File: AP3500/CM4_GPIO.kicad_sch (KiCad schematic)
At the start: 12 parts, among them J9 0826-1X1T-GH-F, U1 TPD4EUSB30, U2 TPD4EUSB30, U5 74LVC1G07SE-7

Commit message: Finalize AP3500 board
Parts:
- added D19, D20, D21, D22, D23, D3: LED Green, LED_SMD:LED_0603_1608Metric, symbol Device:LED
- added J1: Console, Connector_PinHeader_2.54mm:PinHeader_1x04_P2.54mm_Vertical, symbol Connector_Generic:Conn_01x04
- added R19, R20, R36, R39, R6, R7: 1K 1%, Resistor_SMD:R_0603_1608Metric, symbol Device:R
- added U3: SN74LVC07AD, Package_SO:SOIC-14_3.9x8.7mm_P1.27mm, symbol 2021-01-22_15-06-37:SN74LVC07AD
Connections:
- net +3.3v: now also D19.2 (A), D20.2 (A), D21.2 (A), D22.2 (A), D23.2 (A), D3.2 (A), J1.1 (Pin_1), U3.14 (VCC)
- net GND: now also J1.4 (Pin_4), U3.7 (GND)
- net GPIO17: now also U3.9 (4A)
- net GPIO2: now also U3.1 (1A)
- net GPIO22: now also U3.13 (6A)
- net GPIO27: now also U3.11 (5A)
- net GPIO3: now also U3.3 (2A)
- net GPIO4: now also U3.5 (3A)
- net GPIO14 renamed UART_TX
- net UART_TX: now also J1.2 (Pin_2)
- net GPIO15 renamed UART_RX
- net UART_RX: now also J1.3 (Pin_3)
- new net: R36.1, U3.10 (5Y)
- new net: R39.1, U3.12 (6Y)
- new net: R6.1, U3.2 (1Y)
- new net: R7.1, U3.4 (2Y)
- new net: R19.1, U3.6 (3Y)
- new net: R20.1, U3.8 (4Y)
- new net: D22.1 (K), R36.2
- new net: D23.1 (K), R39.2
- new net: D3.1 (K), R6.2
- new net: D21.1 (K), R20.2
- new net: D19.1 (K), R7.2
- new net: D20.1 (K), R19.2
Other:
- note added: "RSSI1 LED"
- note added: "RSSI2 LED"
- note added: "RSSI3 LED"
- note added: "RSSI4 LED"
- note added: "RSSI5 LED"
- note added: "USR LED"

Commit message: More work on Antennas - laying out the new panel as a 2x2 aperture coupled patch
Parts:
- C1: value 100n 16v -> 100n 50v; LCSC (none) -> C14663; PartsBoxID 0603-100nF-X7R-16V -> 0603-100nF-X7R-50V
- D1: LCSC (none) -> C125094; PartsBoxID LTST-S270KRKT -> 0603-LED-RED
- D19, D2, D20, D21, D22, D23, D3: LCSC (none) -> C125094; PartsBoxID LTST-S270KGKT -> 0603-LED-GREEN
- R1, R10, R19, R20, R36, R39, R6, R7: LCSC (none) -> C21190
- R2, R3: LCSC (none) -> C23179
- U3: LCSC (none) -> C7659; PartsBoxID (none) -> SN74LVC07AD
- U5: LCSC (none) -> C7829

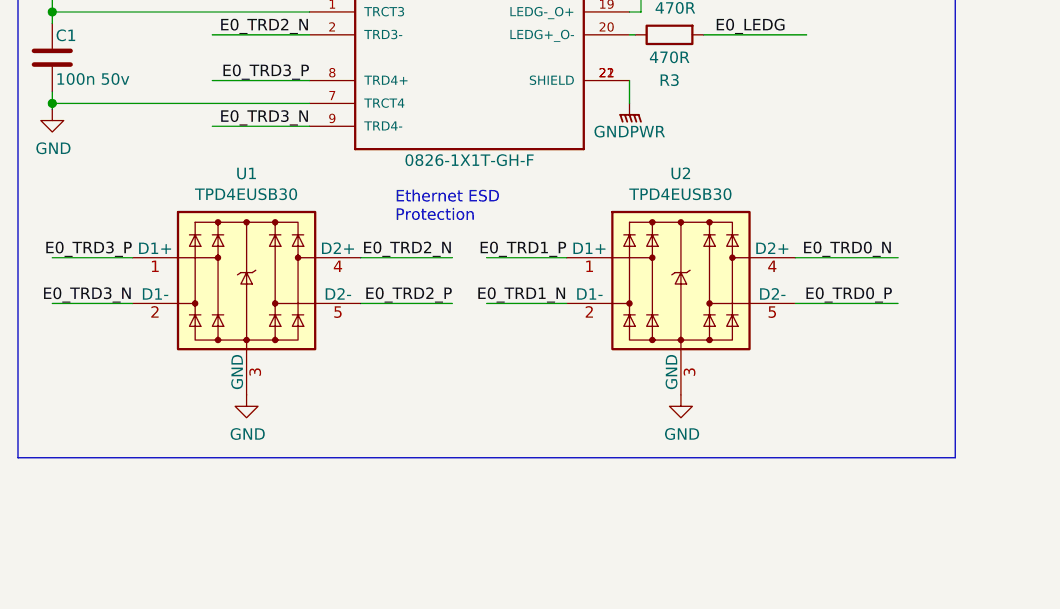
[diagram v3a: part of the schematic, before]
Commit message: Add new single polarity aperture coupled 4x4 antenna. RasPiCNM4Connector test Gerbers for PCBWay Cleanups and optimixations for AP3500
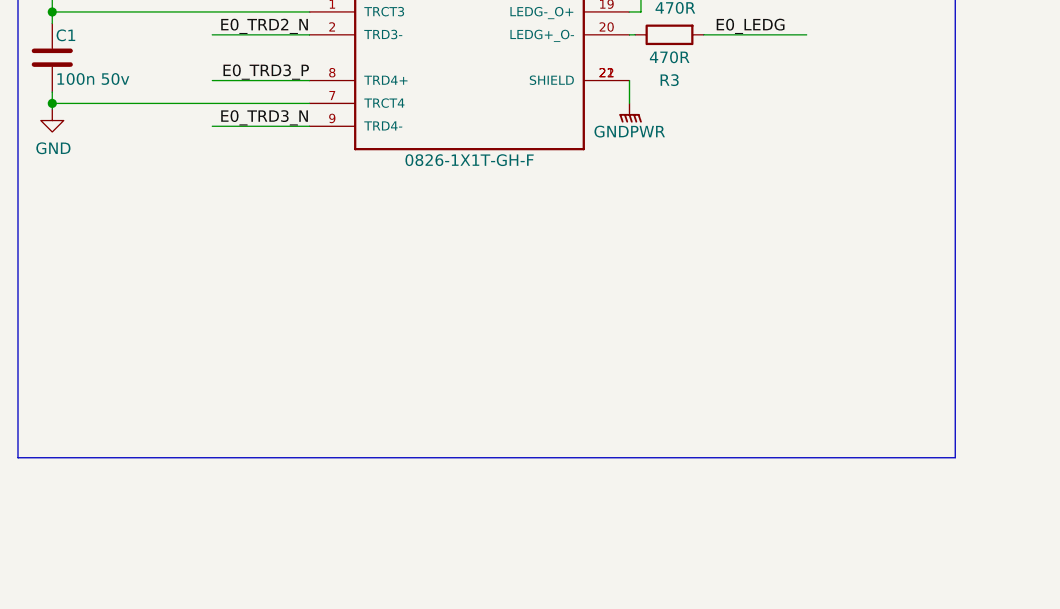
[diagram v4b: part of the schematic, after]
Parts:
- removed U1, U2: TPD4EUSB30, Scott:USON-10_2.51x1.0mm_P0.5mm, symbol AP3500:TPD4EUSB30
- C1: PartsBoxID 0603-100nF-X7R-50V -> (none)
- D1: PartsBoxID 0603-LED-RED -> (none)
- D19, D2, D20, D21, D22, D23, D3: PartsBoxID 0603-LED-GREEN -> (none)
- Module1: footprint AP3500:Raspberry-Pi-4-Compute-Module -> AP3000:Raspberry-Pi-4-Compute-Module; now left out of the parts list
- R1, R10, R19, R20, R36, R39, R6, R7: PartsBoxID 0603-1K-1% -> (none)
- R2, R3: PartsBoxID 0603-470R-1% -> (none)
- U5: PartsBoxID 74LVC1G07SE-7 -> (none)
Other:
- note removed: "Ethernet ESD Protection"

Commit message: Updates for JLCPCB components actually in stock at this time
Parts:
- D1: LCSC C125094 -> C2286
- D19, D2, D20, D21, D22, D23, D3: LCSC C125094 -> C72043
- U5: footprint Package_TO_SOT_SMD:SOT-353_SC-70-5 -> Package_TO_SOT_SMD:SOT-23-5
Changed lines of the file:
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@@
-(kicad_sch (version 20210406) (generator eeschema)
+(kicad_sch (version 20210606) (generator eeschema)
   (paper "A4")
   (title_block
@@
       (effects (font (size 1.27 1.27)) hide)
     )
-    (property "LCSC" "C125094 " (id 10) (at 104.775 146.685 0)
+    (property "LCSC" "C72043" (id 10) (at 104.775 146.685 0)
       (effects (font (size 1.27 1.27)) hide)
     )
@@
       (effects (font (size 1.27 1.27)) hide)
     )
-    (property "LCSC" "C125094 " (id 10) (at 104.775 151.765 0)
+    (property "LCSC" "C72043" (id 10) (at 104.775 151.765 0)
       (effects (font (size 1.27 1.27)) hide)
     )
@@
       (effects (font (size 1.27 1.27)) hide)
     )
-    (property "LCSC" "C125094 " (id 10) (at 104.775 156.845 0)
+    (property "LCSC" "C72043" (id 10) (at 104.775 156.845 0)
       (effects (font (size 1.27 1.27)) hide)
     )
@@
       (effects (font (size 1.27 1.27)) hide)
     )
-    (property "LCSC" "C125094 " (id 10) (at 104.775 161.925 0)
+    (property "LCSC" "C72043" (id 10) (at 104.775 161.925 0)
       (effects (font (size 1.27 1.27)) hide)
     )
@@
       (effects (font (size 1.27 1.27)) hide)
     )
-    (property "LCSC" "C125094 " (id 10) (at 104.775 167.005 0)
+    (property "LCSC" "C72043" (id 10) (at 104.775 167.005 0)
       (effects (font (size 1.27 1.27)) hide)
     )
@@
       (effects (font (size 1.27 1.27)) hide)
     )
-    (property "LCSC" "C125094 " (id 10) (at 104.775 172.085 0)
+    (property "LCSC" "C72043" (id 10) (at 104.775 172.085 0)
       (effects (font (size 1.27 1.27)) hide)
     )
@@
       (effects (font (size 1.27 1.27)) hide)
     )
-    (property "LCSC" "C125094" (id 10) (at 160.02 161.29 0)
+    (property "LCSC" "C2286" (id 10) (at 160.02 161.29 0)
       (effects (font (size 1.27 1.27)) hide)
     )
@@
       (effects (font (size 1.27 1.27)) hide)
     )
-    (property "LCSC" "C125094 " (id 10) (at 225.679 26.67 0)
+    (property "LCSC" "C72043" (id 10) (at 225.679 26.67 0)
       (effects (font (size 1.27 1.27)) hide)
     )
@@
       (effects (font (size 1.27 1.27)) (justify left))
     )
-    (property "Footprint" "Package_TO_SOT_SMD:SOT-353_SC-70-5" (id 2) (at 152.4 180.34 0)
-      (effects (font (size 1.27 1.27)) hide)
-    )
+    (property "Footprint" "Package_TO_SOT_SMD:SOT-23-5" (id 2) (at 152.4 180.34 0)
+      (effects (font (size 1.27 1.27)) hide)
+    )

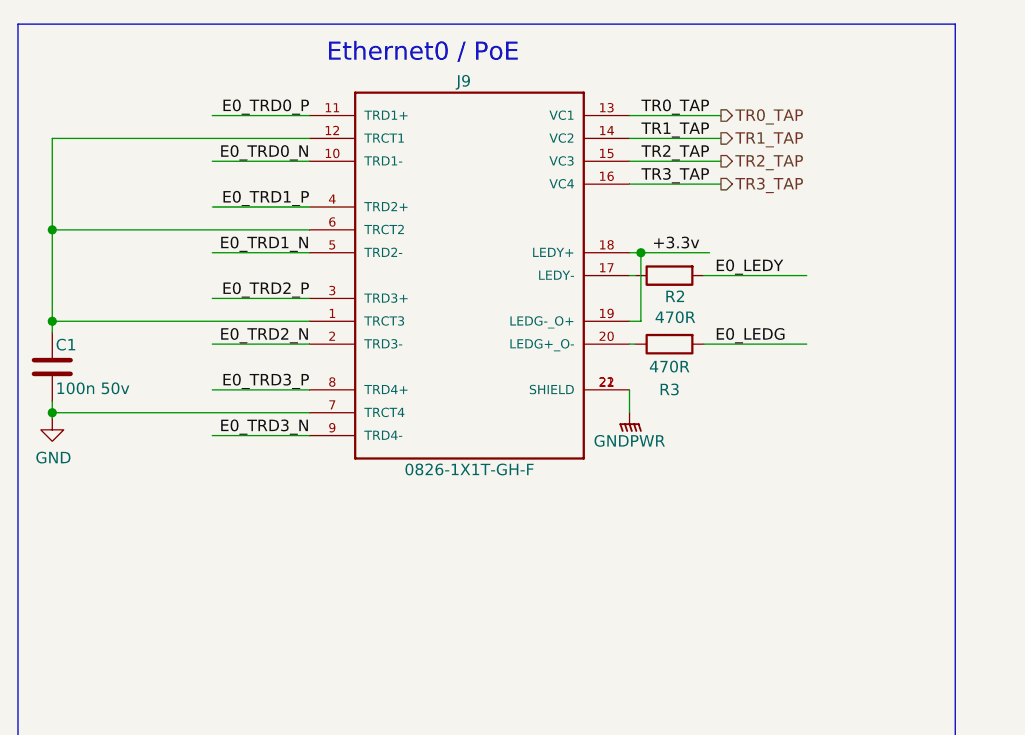
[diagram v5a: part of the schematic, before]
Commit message: Update AP3500 with new Wurth footprint - needed rerouted. Fix the gigabit ethernet problem with pair 4 center tap to ground instead of through cap.
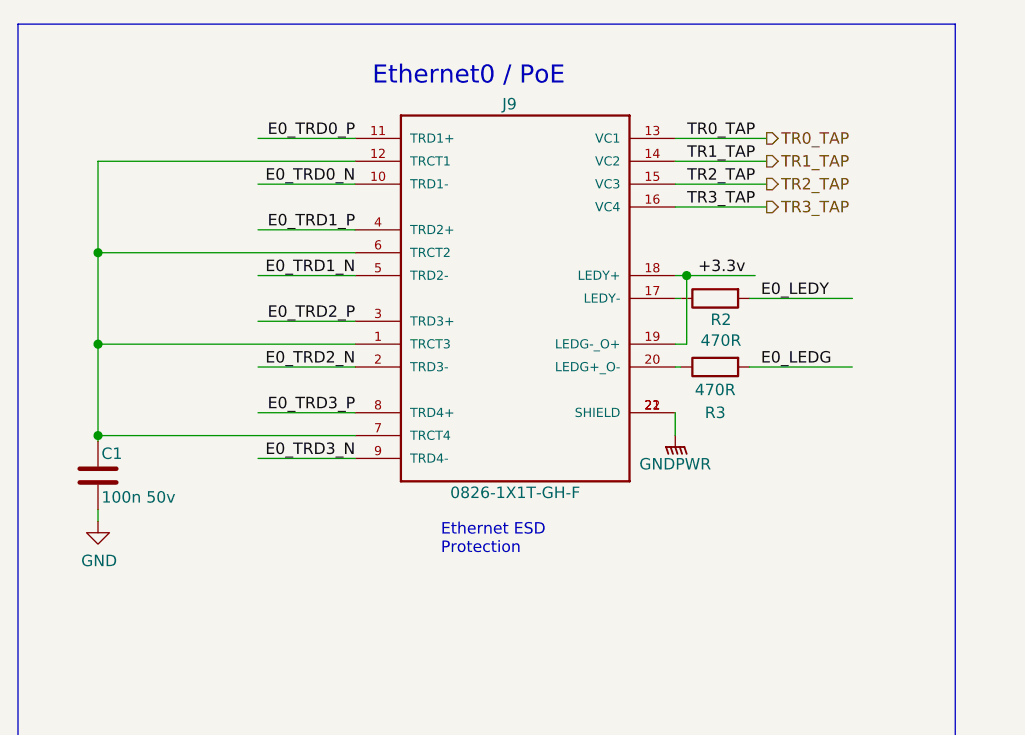
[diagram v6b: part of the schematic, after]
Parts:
- C1: Part Description 0.1uF 10% 16V Ceramic Capacitor X7R 0402 (1005 Metric) -> 100nF 10% or 20% 50V Ceramic Capacitor X7R 0603; PartsBoxID (none) -> 0603-100nF-X7R-50V
- R2, R3: PartsBoxID (none) -> 0603-470R-1%
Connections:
- net GND: no longer J9.7 (TRCT4)
- net at C1.1, J9.1 (TRCT3), J9.12 (TRCT1)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: now also J9.7 (TRCT4)
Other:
- note added: "Ethernet ESD Protection"
